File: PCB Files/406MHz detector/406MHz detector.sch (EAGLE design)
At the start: 26 parts, among them J1 switch

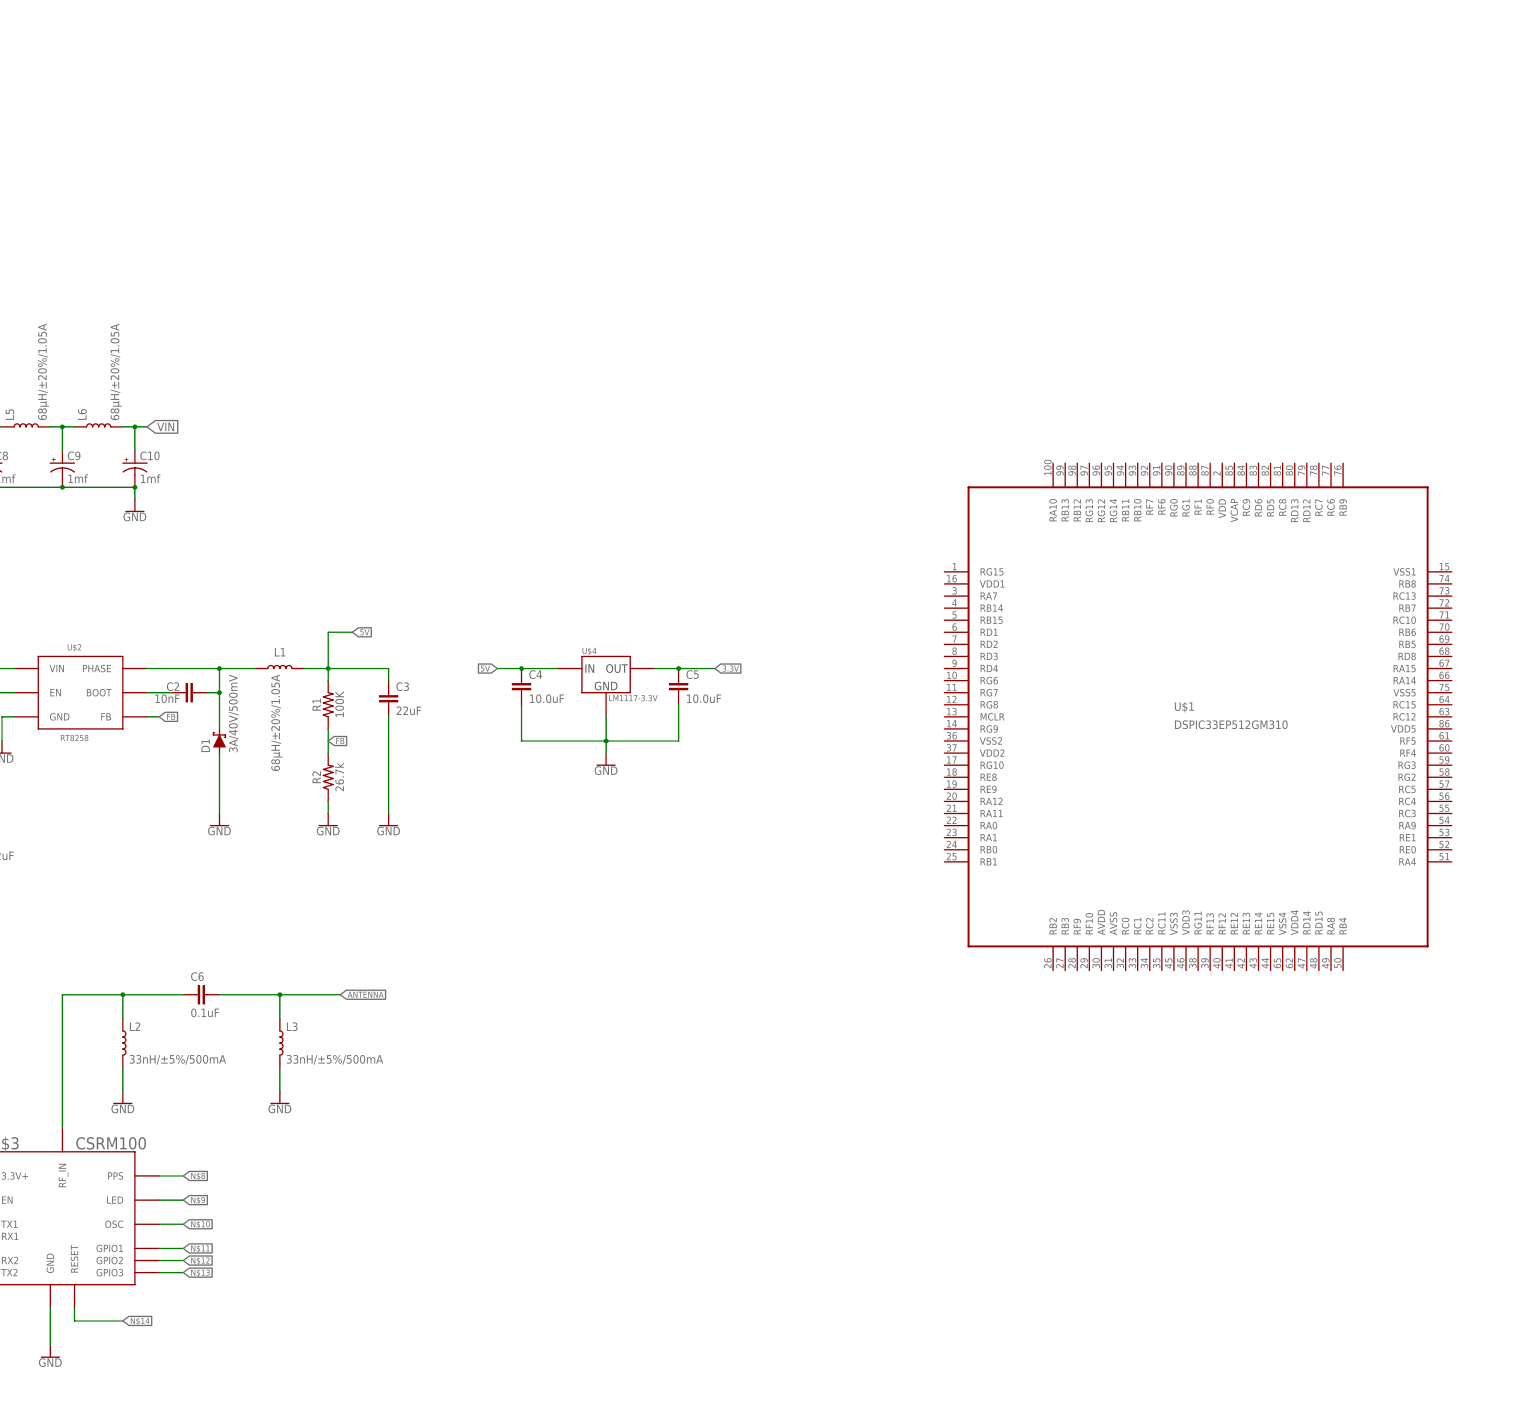
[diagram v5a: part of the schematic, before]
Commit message: changed uc, added crystal
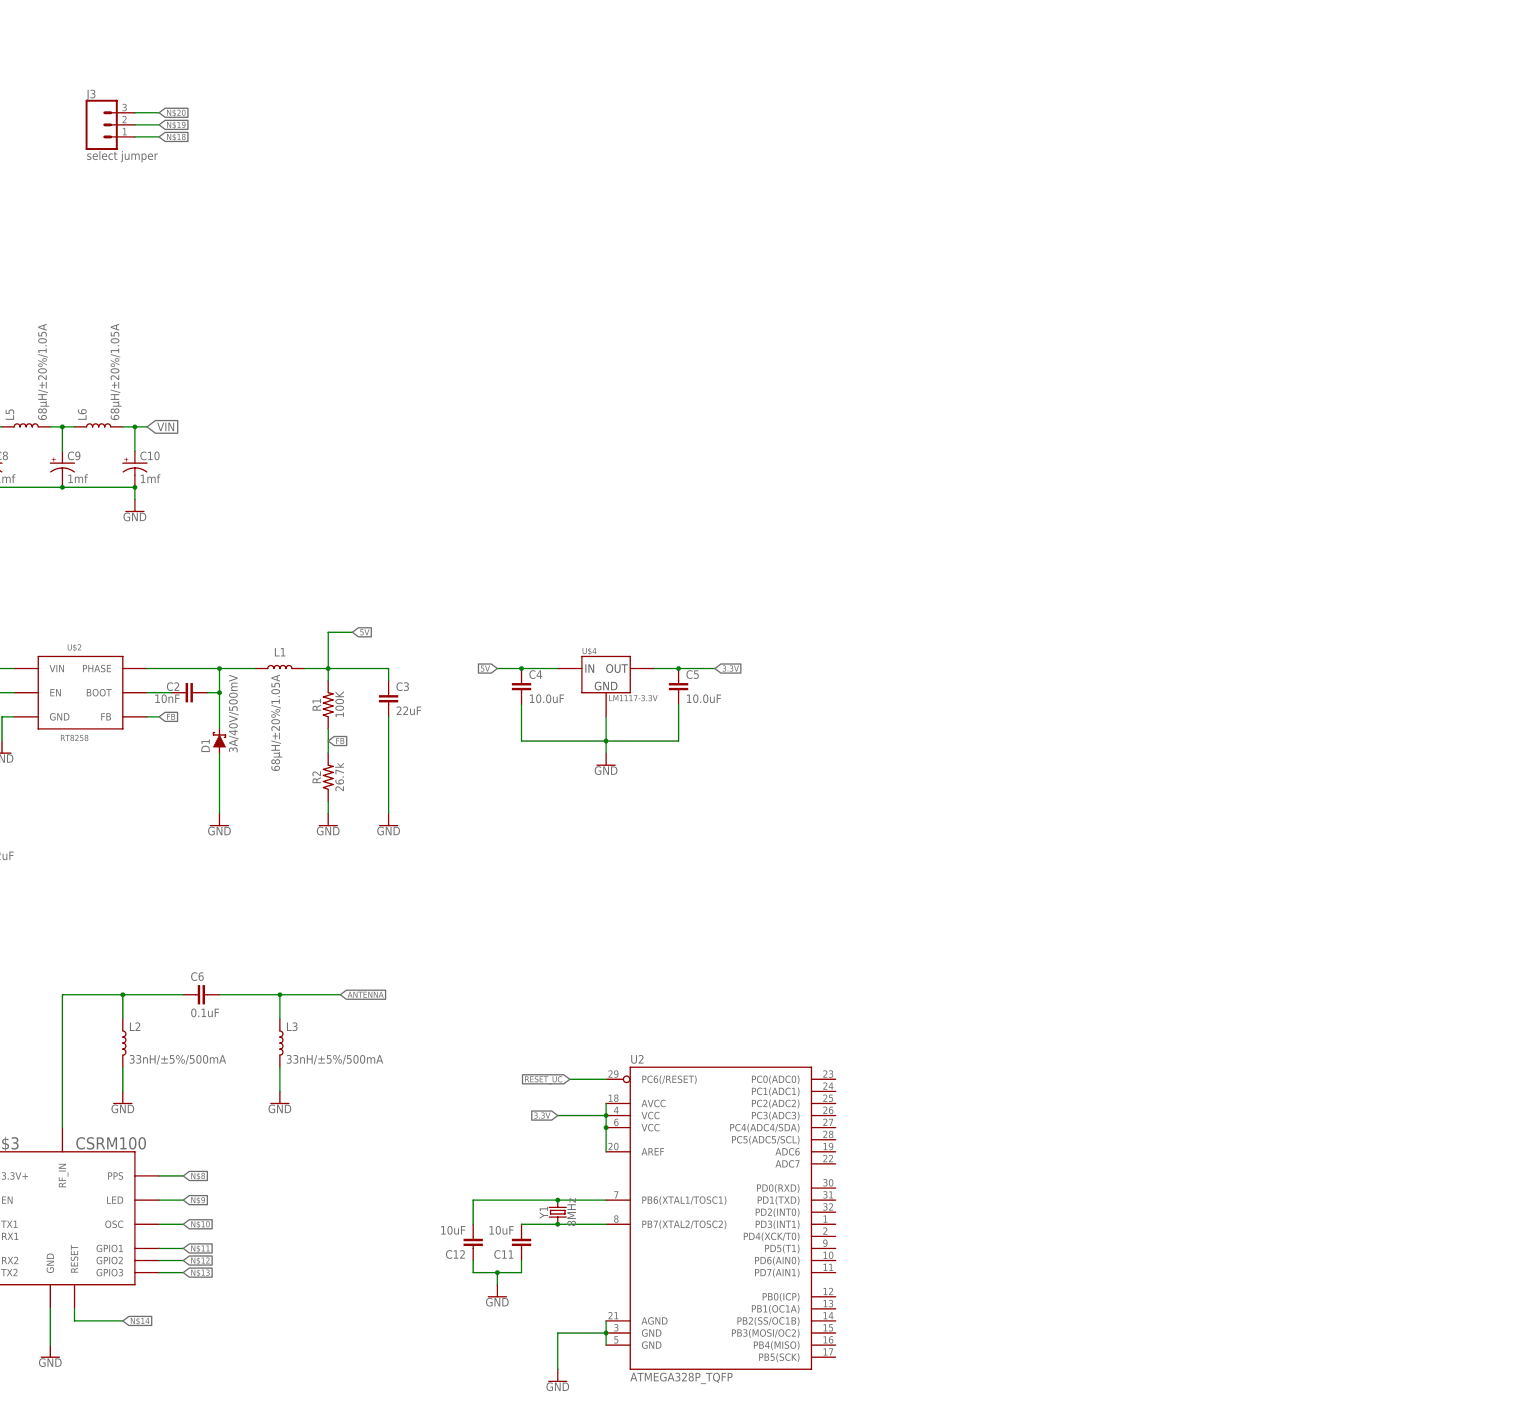
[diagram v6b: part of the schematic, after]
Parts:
- removed U$1: DSPIC33EP512GM310, capstone:DSPIC33EP512GM310
- added C11, C12: 10uF, SparkFun-Capacitors:10UF-1206-6.3V-20%
- added J3: select jumper, SparkFun-Connectors:CONN_03LOCK
- added U2: ATMEGA328P_TQFP, SparkFun-IC-Microcontroller:ATMEGA328P_TQFP
- added Y1: 8MHz, SparkFun-Clocks:CRYSTAL-8MHZSMD-HC49UP
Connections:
- new net N$18: J3.1
- new net N$19: J3.2
- new net N$20: J3.3
- new net N$21: C12.2, U2.PB6(XTAL1/TOSC1), Y1.2
- new net N$22: C11.2, U2.PB7(XTAL2/TOSC2), Y1.1
- new net RESET_UC: U2.PC6(/RESET)
- net 3.3V: now also U2.AREF, U2.AVCC, U2.VCC@4, U2.VCC@6
- net GND: now also C11.1, C12.1, U2.AGND, U2.GND@3, U2.GND@5
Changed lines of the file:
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@@
 </classes>
 <parts>
-<part name="U$1" library="capstone" deviceset="DSPIC33EP512GM310" device=""/>
 <part name="U$2" library="capstone" deviceset="RT8258" device=""/>
 <part name="C1" library="SparkFun-Capacitors" library_urn="urn:adsk.eagle:library:510" deviceset="10NF" device="-0603-50V-10%" package3d_urn="urn:adsk.eagle:package:37414/1" value="10nF"/>
@@
 <part name="J2" library="SparkFun-Connectors" library_urn="urn:adsk.eagle:library:513" deviceset="CONN_02" device="LOCK" package3d_urn="urn:adsk.eagle:package:38045/1"/>
 <part name="GND12" library="SparkFun-PowerSymbols" library_urn="urn:adsk.eagle:library:530" deviceset="GND" device=""/>
+<part name="U2" library="SparkFun-IC-Microcontroller" library_urn="urn:adsk.eagle:library:525" deviceset="ATMEGA328P_TQFP" device="" package3d_urn="urn:adsk.eagle:package:38945/1" value="ATMEGA328P_TQFP"/>
+<part name="GND13" library="SparkFun-PowerSymbols" library_urn="urn:adsk.eagle:library:530" deviceset="GND" device=""/>
+<part name="J3" library="SparkFun-Connectors" library_urn="urn:adsk.eagle:library:513" deviceset="CONN_03" device="LOCK" package3d_urn="urn:adsk.eagle:package:38071/1" value="select jumper"/>
+<part name="Y1" library="SparkFun-Clocks" library_urn="urn:adsk.eagle:library:511" deviceset="CRYSTAL-8MHZ" device="SMD-HC49UP" package3d_urn="urn:adsk.eagle:package:37513/1" value="8MHz"/>
+<part name="C11" library="SparkFun-Capacitors" library_urn="urn:adsk.eagle:library:510" deviceset="10UF" device="-1206-6.3V-20%" package3d_urn="urn:adsk.eagle:package:37426/1" value="10uF"/>
+<part name="C12" library="SparkFun-Capacitors" library_urn="urn:adsk.eagle:library:510" deviceset="10UF" device="-1206-6.3V-20%" package3d_urn="urn:adsk.eagle:package:37426/1" value="10uF"/>
+<part name="GND14" library="SparkFun-PowerSymbols" library_urn="urn:adsk.eagle:library:530" deviceset="GND" device=""/>
 </parts>
 <sheets>
@@
 </plain>
 <instances>
-<instance part="U$1" gate="G$1" x="312.42" y="175.26" smashed="yes">
-<attribute name="NAME" x="307.34" y="176.53" size="1.778" layer="95"/>
-<attribute name="VALUE" x="307.34" y="172.72" size="1.778" layer="96"/>
-</instance>
 <instance part="U$2" gate="G$1" x="76.2" y="180.34" smashed="yes">
 <attribute name="NAME" x="76.2" y="189.23" size="1.27" layer="95" align="bottom-center"/>
@@
 <instance part="GND12" gate="1" x="30.48" y="287.02" smashed="yes">
 <attribute name="VALUE" x="30.48" y="286.766" size="1.778" layer="96" align="top-center"/>
+</instance>
+<instance part="U2" gate="U$1" x="213.36" y="68.58" smashed="yes">
+<attribute name="NAME" x="193.04" y="102.362" size="1.778" layer="95"/>
+<attribute name="VALUE" x="193.04" y="35.56" size="1.778" layer="96"/>
+</instance>
+<instance part="GND13" gate="1" x="177.8" y="35.56" smashed="yes">
+<attribute name="VALUE" x="177.8" y="35.306" size="1.778" layer="96" align="top-center"/>
+</instance>
+<instance part="J3" gate="J$1" x="81.28" y="299.72" smashed="yes">
+<attribute name="VALUE" x="78.74" y="292.354" size="1.778" layer="96" font="vector"/>
+<attribute name="NAME" x="78.74" y="305.308" size="1.778" layer="95" font="vector"/>
+</instance>
+<instance part="Y1" gate="G$1" x="177.8" y="71.12" smashed="yes" rot="R90">
+<attribute name="NAME" x="175.768" y="71.12" size="1.778" layer="95" font="vector" rot="R90" align="bottom-center"/>
+<attribute name="VALUE" x="179.832" y="71.12" size="1.778" layer="96" font="vector" rot="R90" align="top-center"/>
+</instance>
+<instance part="C11" gate="G$1" x="170.18" y="66.04" smashed="yes" rot="R180">
+<attribute name="NAME" x="168.656" y="63.119" size="1.778" layer="95" font="vector" rot="R180"/>
+<attribute name="VALUE" x="168.656" y="68.199" size="1.778" layer="96" font="vector" rot="R180"/>
+</instance>
+<instance part="C12" gate="G$1" x="160.02" y="66.04" smashed="yes" rot="R180">
+<attribute name="NAME" x="158.496" y="63.119" size="1.778" layer="95" font="vector" rot="R180"/>
+<attribute name="VALUE" x="158.496" y="68.199" size="1.778" layer="96" font="vector" rot="R180"/>
+</instance>
+<instance part="GND14" gate="1" x="165.1" y="53.34" smashed="yes">
+<attribute name="VALUE" x="165.1" y="53.086" size="1.778" layer="96" align="top-center"/>
 </instance>
 </instances>
@@
 <label x="210.82" y="185.42" size="1.27" layer="95" xref="yes"/>
 <pinref part="U$4" gate="G$1" pin="VOUT"/>
+</segment>
+<segment>
+<pinref part="U2" gate="U$1" pin="AVCC"/>
+<pinref part="U2" gate="U$1" pin="VCC@4"/>
+<wire x1="187.96" y1="93.98" x2="187.96" y2="91.44" width="0.1524" layer="91"/>
+<pinref part="U2" gate="U$1" pin="VCC@6"/>
+<wire x1="187.96" y1="91.44" x2="187.96" y2="88.9" width="0.1524" layer="91"/>
+<junction x="187.96" y="91.44"/>
+<wire x1="187.96" y1="91.44" x2="177.8" y2="91.44" width="0.1524" layer="91"/>
+<label x="177.8" y="91.44" size="1.27" layer="95" rot="R180" xref="yes"/>
+<pinref part="U2" gate="U$1" pin="AREF"/>
+<wire x1="187.96" y1="83.82" x2="187.96" y2="88.9" width="0.1524" layer="91"/>
+<junction x="187.96" y="88.9"/>
 </segment>
 </net>
@@
 <pinref part="GND12" gate="1" pin="GND"/>
 </segment>
+<segment>
+<wire x1="187.96" y1="48.26" x2="187.96" y2="45.72" width="0.1524" layer="91"/>
+<wire x1="187.96" y1="43.18" x2="187.96" y2="45.72" width="0.1524" layer="91"/>
+<junction x="187.96" y="45.72"/>
+<wire x1="187.96" y1="45.72" x2="177.8" y2="45.72" width="0.1524" layer="91"/>
+<wire x1="177.8" y1="45.72" x2="177.8" y2="38.1" width="0.1524" layer="91"/>
+<pinref part="U2" gate="U$1" pin="GND@3"/>
+<pinref part="U2" gate="U$1" pin="GND@5"/>
+<pinref part="U2" gate="U$1" pin="AGND"/>
+<pinref part="GND13" gate="1" pin="GND"/>
+</segment>
+<segment>
+<pinref part="C11" gate="G$1" pin="1"/>
+<wire x1="170.18" y1="60.96" x2="170.18" y2="58.42" width="0.1524" layer="91"/>
+<wire x1="170.18" y1="58.42" x2="165.1" y2="58.42" width="0.1524" layer="91"/>
+<pinref part="C12" gate="G$1" pin="1"/>
+<wire x1="165.1" y1="58.42" x2="160.02" y2="58.42" width="0.1524" layer="91"/>
+<wire x1="160.02" y1="58.42" x2="160.02" y2="60.96" width="0.1524" layer="91"/>
+<wire x1="165.1" y1="58.42" x2="165.1" y2="55.88" width="0.1524" layer="91"/>
+<junction x="165.1" y="58.42"/>
+<pinref part="GND14" gate="1" pin="GND"/>
+</segment>
 </net>
 <net name="N$1" class="0">
@@
 </segment>
 </net>
+<net name="N$18" class="0">
+<segment>
+<pinref part="J3" gate="J$1" pin="1"/>
+<wire x1="88.9" y1="297.18" x2="93.98" y2="297.18" width="0.1524" layer="91"/>
+<label x="93.98" y="297.18" size="1.27" layer="95" xref="yes"/>
+</segment>
+</net>
+<net name="N$19" class="0">
+<segment>
+<pinref part="J3" gate="J$1" pin="2"/>
+<wire x1="88.9" y1="299.72" x2="93.98" y2="299.72" width="0.1524" layer="91"/>
+<label x="93.98" y="299.72" size="1.27" layer="95" xref="yes"/>
+</segment>
+</net>
+<net name="N$20" class="0">
+<segment>
+<pinref part="J3" gate="J$1" pin="3"/>
+<wire x1="88.9" y1="302.26" x2="93.98" y2="302.26" width="0.1524" layer="91"/>
+<label x="93.98" y="302.26" size="1.27" layer="95" xref="yes"/>
+</segment>
+</net>
+<net name="RESET_UC" class="0">
+<segment>
+<pinref part="U2" gate="U$1" pin="PC6(/RESET)"/>
+<wire x1="187.96" y1="99.06" x2="180.34" y2="99.06" width="0.1524" layer="91"/>
+<label x="180.34" y="99.06" size="1.27" layer="95" rot="R180" xref="yes"/>
+</segment>
+</net>
+<net name="N$21" class="0">
+<segment>
+<pinref part="U2" gate="U$1" pin="PB6(XTAL1/TOSC1)"/>
+<pinref part="Y1" gate="G$1" pin="2"/>
+<wire x1="187.96" y1="73.66" x2="177.8" y2="73.66" width="0.1524" layer="91"/>
+<wire x1="177.8" y1="73.66" x2="160.02" y2="73.66" width="0.1524" layer="91"/>
+<junction x="177.8" y="73.66"/>
+<pinref part="C12" gate="G$1" pin="2"/>
+<wire x1="160.02" y1="73.66" x2="160.02" y2="68.58" width="0.1524" layer="91"/>
+</segment>
+</net>
+<net name="N$22" class="0">
+<segment>
+<pinref part="C11" gate="G$1" pin="2"/>
+<pinref part="Y1" gate="G$1" pin="1"/>
+<wire x1="170.18" y1="68.58" x2="177.8" y2="68.58" width="0.1524" layer="91"/>
+<pinref part="U2" gate="U$1" pin="PB7(XTAL2/TOSC2)"/>
+<wire x1="187.96" y1="68.58" x2="177.8" y2="68.58" width="0.1524" layer="91"/>
+<junction x="177.8" y="68.58"/>
+</segment>
+</net>
